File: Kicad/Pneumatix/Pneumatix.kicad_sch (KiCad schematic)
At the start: 22 parts, among them J1 Conn_01x06_Socket, J2 436500404, J3 142-0701-801, U1 E22-400T33S

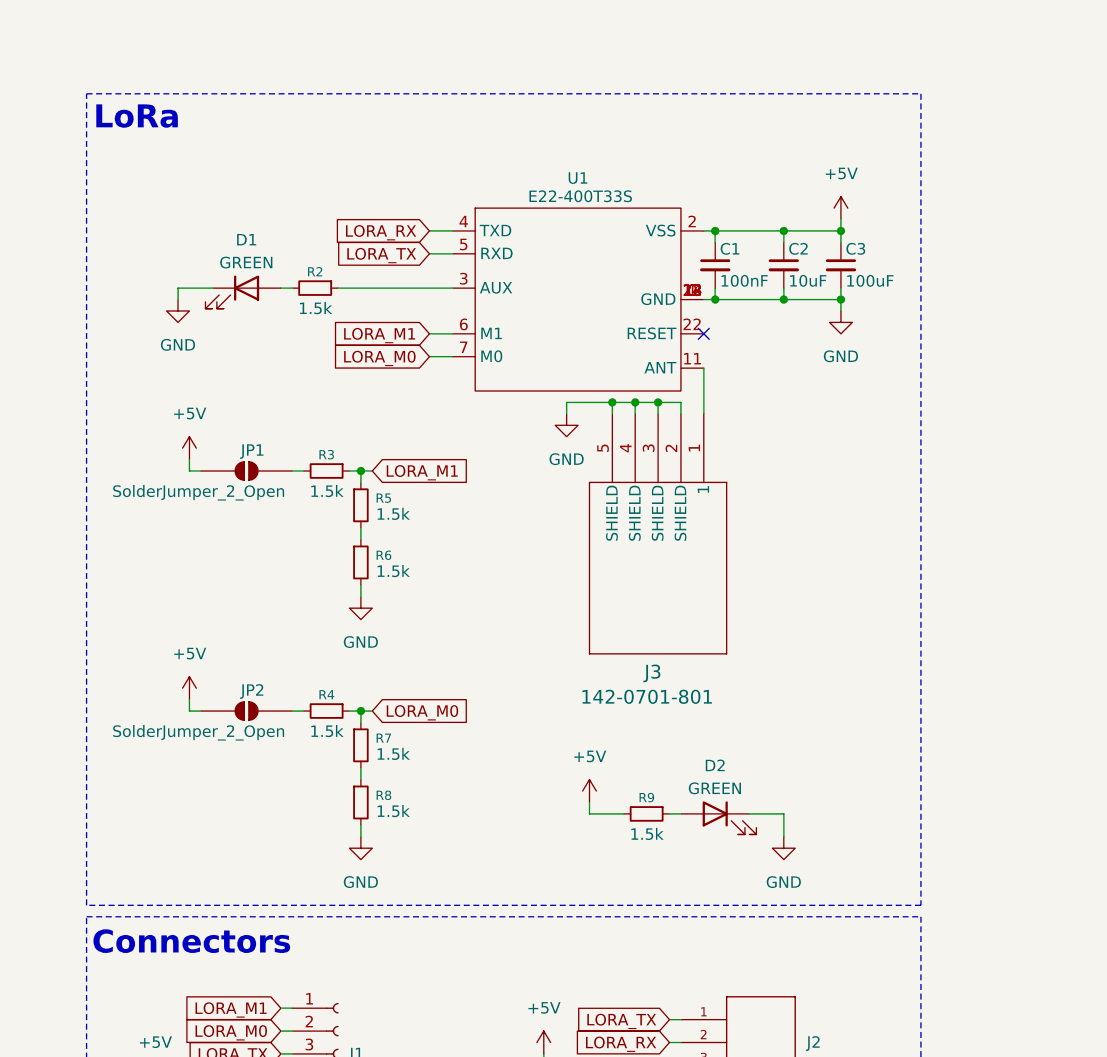
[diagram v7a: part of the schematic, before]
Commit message: wip: change 100uF cap to 220uF, add component fields and fix routing for new cap
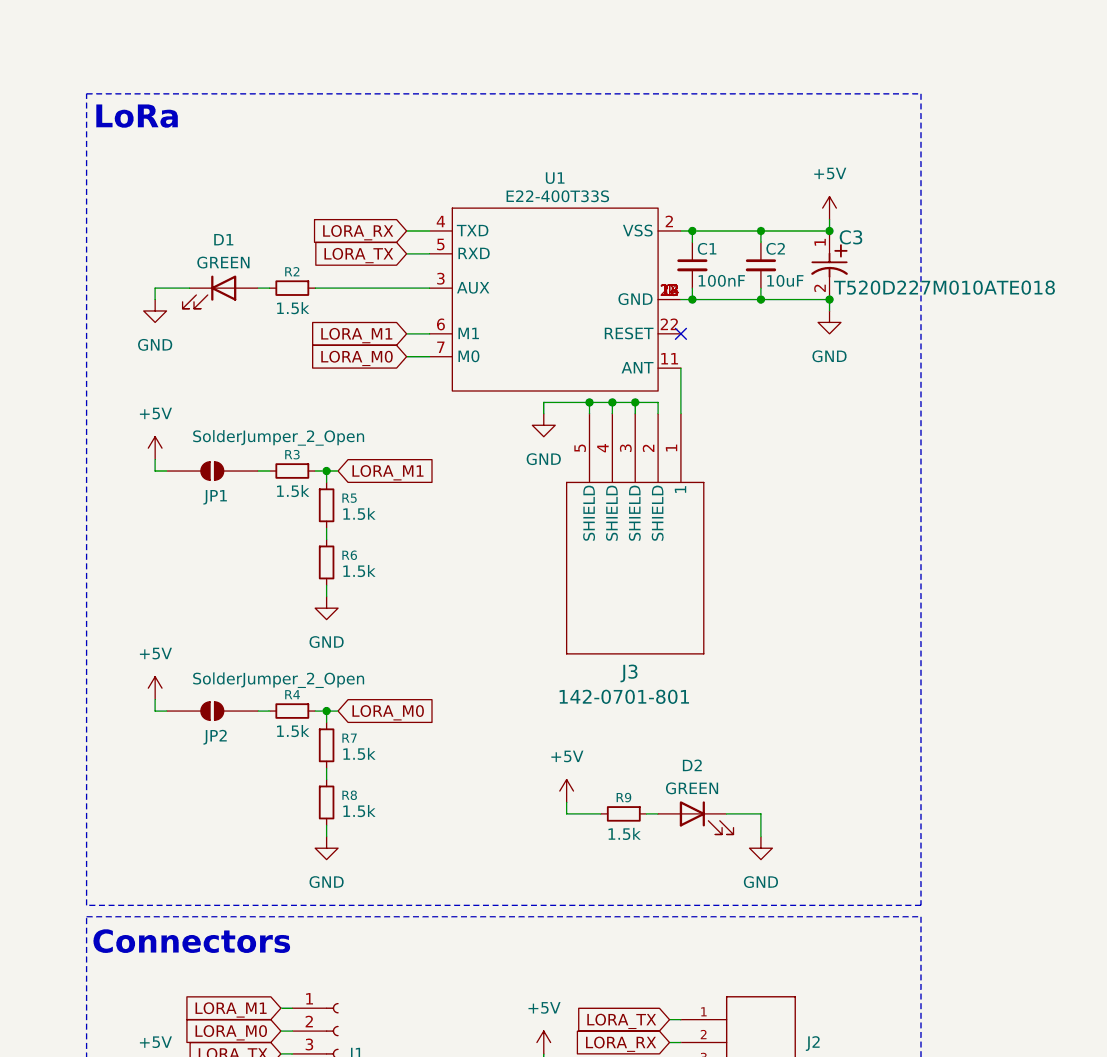
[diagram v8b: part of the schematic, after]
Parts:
- removed C3: 100uF, Capacitor_SMD:C_0603_1608Metric, symbol Device:C_Small
- added C3: T520D227M010ATE018, Pneumatix_Lib:CAPMP7.6X4.3_3.1N_KEM, symbol Pneumatix_Lib:T520D227M010ATE018
- C1: DigitKey_Part_Number (none) -> 399-C0603C104K5RACTUCT-ND; Manufacturer_Part_Number (none) -> C0603C104K5RACTU
- C2: DigitKey_Part_Number (none) -> 587-3258-1-ND; Manufacturer_Part_Number (none) -> LMK107BBJ106MALT
- D1, D2: DigitKey_Part_Number (none) -> 160-LTST-C190GKTCT-ND; Manufacturer_Part_Number (none) -> LTST-C190GKT
- J2: DigitKey_Part_Number (none) -> WM1877-ND; Manufacturer_Part_Number (none) -> 0436500404
- J3: DigitKey_Part_Number (none) -> J502-ND; Manufacturer_Part_Number (none) -> 142-0701-801
- R2, R3, R4, R5, R6, R7, R8, R9: DigitKey_Part_Number (none) -> RG16P1.5KBCT-ND; Manufacturer_Part_Number (none) -> RG1608P-152-B-T5
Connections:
- net +5V: now also C3.1
- net GND: now also C3.2
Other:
- moved on the sheet: C1, C2, D1, D2, J3, JP1, JP2, R2, R3, R4, R5, R6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
